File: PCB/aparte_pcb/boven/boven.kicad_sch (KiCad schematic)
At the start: 47 parts, among them IC1 TSSP4038, IC10 TSSP4038, IC11 TSSP4038, IC12 TSSP4038, IC13 TSSP4038, IC14 TSSP4038, IC15 TSSP4038, IC16 TSSP4038, IC2 TSSP4038, IC3 TSSP4038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

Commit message: Add files via upload
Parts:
- added J1: Conn_01x10_Socket, Connector_JST:JST_EH_S10B-EH_1x10_P2.50mm_Horizontal, symbol Connector:Conn_01x10_Socket
- IC1, IC10, IC11, IC12, IC13, IC14, IC15, IC16, IC2, IC3, IC4, IC5, IC6, IC7, IC8, IC9: footprint irsens:TSSP4038 -> Library:TSSP4038
- IR_controller1, IR_controller2: footprint Seeed Studio XIAO Series Library:XIAO-SAMD21-RP2040-14P-2.54-21X17.8MM (Seeeduino XIAO) -> Library:Seeduino Xiao Kicad af
- SW1: footprint (none) -> Library:R1966ABLKBLKEF
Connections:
- net 3v3: now also J1.2 (Pin_2)
- net 5v: now also J1.1 (Pin_1)
- net gnd: now also J1.3 (Pin_3)
- net rx1: now also J1.5 (Pin_5)
- net rx2: now also J1.7 (Pin_7)
- net rx3: now also J1.9 (Pin_9)
- net soft_power_sw: now also J1.10 (Pin_10)
- net tx1: now also J1.4 (Pin_4)
- net tx2: now also J1.6 (Pin_6)
- net tx3: now also J1.8 (Pin_8)
- net at IR_controller1.10 (PA5_A9_D9_MISO): now also IC3.1 (OUT)
- net at IR_controller2.10 (PA5_A9_D9_MISO): now also IC11.1 (OUT)

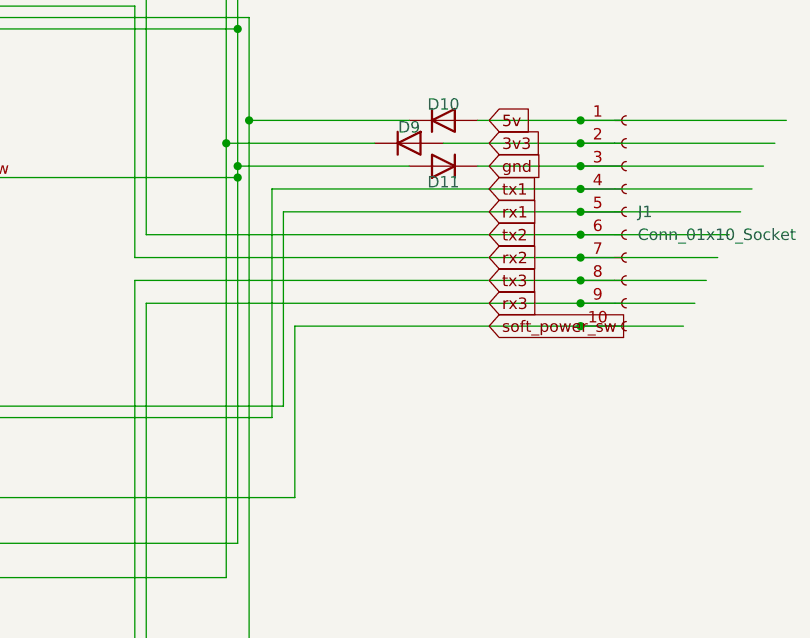
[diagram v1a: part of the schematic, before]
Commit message: schroef geaard
moet nog onderste schroef
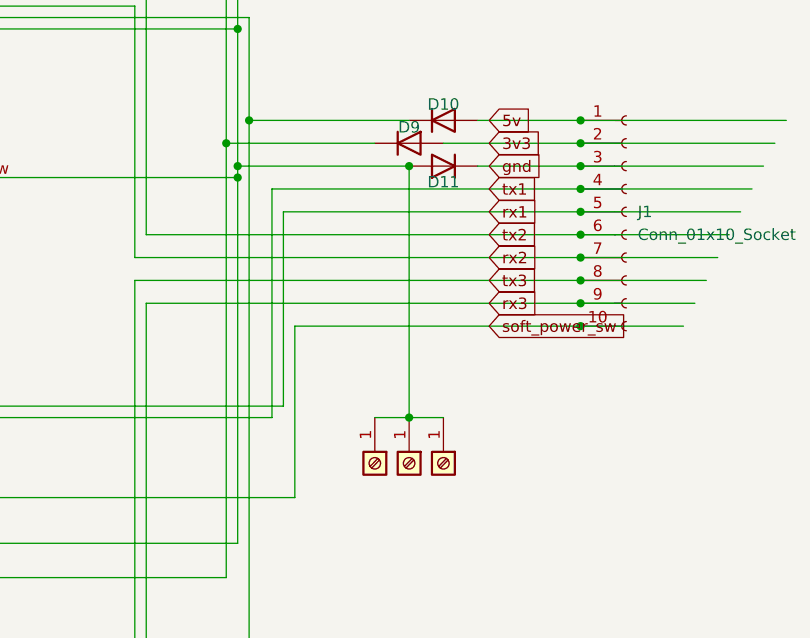
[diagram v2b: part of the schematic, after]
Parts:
- added J2: Screw_Terminal_01x01, MountingHole:MountingHole_4.3mm_M4_DIN965_Pad, symbol Connector:Screw_Terminal_01x01
- added J3, J4: Screw_Terminal_01x01, MountingHole:MountingHole_4.3mm_M4_ISO7380_Pad, symbol Connector:Screw_Terminal_01x01
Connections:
- net at D11.2 (A), D2.1 (K), D3.1 (K)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: now also J2.1 (Pin_1), J3.1 (Pin_1), J4.1 (Pin_1)
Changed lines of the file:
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@@
 	)
 	(junction
+		(at 205.74 107.95)
+		(diameter 0)
+		(color 0 0 0 0)
+	)
+	(junction
 		(at 50.8 105.41)
 		(diameter 0)
@@
 	)
 	(junction
+		(at 205.74 80.01)
+		(diameter 0)
+		(color 0 0 0 0)
+	)
+	(junction
 		(at 52.07 46.99)
 		(diameter 0)
@@
 	(wire
 		(pts
+			(xy 205.74 80.01) (xy 205.74 107.95)
+		)
+		(stroke
+			(width 0)
+			(type default)
+		)
+	)
+	(wire
+		(pts
 			(xy 52.07 67.31) (xy 52.07 77.47)
 		)
@@
 	(wire
 		(pts
+			(xy 201.93 107.95) (xy 205.74 107.95)
+		)
+		(stroke
+			(width 0)
+			(type default)
+		)
+	)
+	(wire
+		(pts
+			(xy 205.74 107.95) (xy 209.55 107.95)
+		)
+		(stroke
+			(width 0)
+			(type default)
+		)
+	)
+	(wire
+		(pts
 			(xy 52.07 46.99) (xy 52.07 36.83)
 		)
@@
 	)
 	(symbol
+		(lib_id "Connector:Screw_Terminal_01x01")
+		(at 205.74 113.03 270)
+		(unit 1)
+		(exclude_from_sim no)
+		(in_bom yes)
+		(on_board yes)
+		(dnp no)
+		(fields_autoplaced yes)
+		(property "Reference" "J3"
+			(at 207.0101 115.57 0)
+			(effects
+				(font
+					(size 1.27 1.27)
+				)
+				(justify left)
+				(hide yes)
+			)
+		)
+		(property "Value" "Screw_Terminal_01x01"
+			(at 204.4701 115.57 0)
+			(effects
+				(font
+					(size 1.27 1.27)
+				)
+				(justify left)
+				(hide yes)
+			)
+		)
+		(property "Footprint" "MountingHole:MountingHole_4.3mm_M4_ISO7380_Pad"
+			(at 205.74 113.03 0)
+			(effects
+				(font
+					(size 1.27 1.27)
+				)
+				(hide yes)
+			)
+		)
+		(property "Datasheet" "~"
+			(at 205.74 113.03 0)
+			(effects
+				(font
+					(size 1.27 1.27)
+				)
+				(hide yes)
+			)
+		)
+		(property "Description" "Generic screw terminal, single row, 01x01, script generated (kicad-library-utils/schlib/autogen/connector/)"
+			(at 205.74 113.03 0)
+			(effects
+				(font
+					(size 1.27 1.27)
+				)
+				(hide yes)
+			)
+		)
+		(pin "1"
+		)
+		(instances
+			(project "boven"
+				(path "/9e41cf64-9ee8-413c-ad53-0190c7714871"
+					(reference "J3")
+					(unit 1)
+				)
+			)
+		)
+	)
+	(symbol
 		(lib_id "Library:openMV_M7_R2")
 		(at 135.89 87.63 90)
@@
 	)
 	(symbol
+		(lib_id "Connector:Screw_Terminal_01x01")
+		(at 201.93 113.03 270)
+		(unit 1)
+		(exclude_from_sim no)
+		(in_bom yes)
+		(on_board yes)
+		(dnp no)
+		(fields_autoplaced yes)
+		(property "Reference" "J4"
+			(at 203.2001 115.57 0)
+			(effects
+				(font
+					(size 1.27 1.27)
+				)
+				(justify left)
+				(hide yes)
+			)
+		)
+		(property "Value" "Screw_Terminal_01x01"
+			(at 200.6601 115.57 0)
+			(effects
+				(font
+					(size 1.27 1.27)
+				)
+				(justify left)
+				(hide yes)
+			)
+		)
+		(property "Footprint" "MountingHole:MountingHole_4.3mm_M4_ISO7380_Pad"
+			(at 201.93 113.03 0)
+			(effects
+				(font
+					(size 1.27 1.27)
+				)
+				(hide yes)
+			)
+		)
+		(property "Datasheet" "~"
+			(at 201.93 113.03 0)
+			(effects
+				(font
+					(size 1.27 1.27)
+				)
+				(hide yes)
+			)
+		)
+		(property "Description" "Generic screw terminal, single row, 01x01, script generated (kicad-library-utils/schlib/autogen/connector/)"
+			(at 201.93 113.03 0)
+			(effects
+				(font
+					(size 1.27 1.27)
+				)
+				(hide yes)
+			)
+		)
+		(pin "1"
+		)
+		(instances
+			(project "boven"
+				(path "/9e41cf64-9ee8-413c-ad53-0190c7714871"
+					(reference "J4")
+					(unit 1)
+				)
+			)
+		)
+	)
+	(symbol
 		(lib_id "Library:R_US")
 		(at 46.99 85.09 90)
@@
 					(unit 1)
 				)
+			)
+		)
+	)
+	(symbol
+		(lib_id "Connector:Screw_Terminal_01x01")
+		(at 209.55 113.03 270)
+		(unit 1)
+		(exclude_from_sim no)
+		(in_bom yes)
+		(on_board yes)
+		(dnp no)
+		(fields_autoplaced yes)
+		(property "Reference" "J2"
+			(at 210.8201 115.57 0)
+			(effects
+				(font
+					(size 1.27 1.27)
+				)
+				(justify left)
+				(hide yes)
+			)
+		)
+		(property "Value" "Screw_Terminal_01x01"
+			(at 208.2801 115.57 0)
+			(effects
+				(font
+					(size 1.27 1.27)
+				)
+				(justify left)
+				(hide yes)
+			)
+		)
+		(property "Footprint" "MountingHole:MountingHole_4.3mm_M4_DIN965_Pad"
+			(at 209.55 113.03 0)
+			(effects
+				(font
+					(size 1.27 1.27)
+				)
+				(hide yes)
+			)
+		)
+		(property "Datasheet" "~"
+			(at 209.55 113.03 0)
+			(effects
+				(font
+					(size 1.27 1.27)
+				)
+				(hide yes)
+			)
+		)
+		(property "Description" "Generic screw terminal, single row, 01x01, script generated (kicad-library-utils/schlib/autogen/connector/)"
+			(at 209.55 113.03 0)
+			(effects
+				(font
+					(size 1.27 1.27)
+				)
+				(hide yes)
+			)
+		)
+		(pin "1"
+		)
+		(instances
+			(project ""
+				(path "/9e41cf64-9ee8-413c-ad53-0190c7714871"
+					(reference "J2")
+					(unit 1)
+				)
